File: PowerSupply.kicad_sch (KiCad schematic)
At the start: 9 parts, among them Q1 DMP2160UW-7, U1 MIC2288YD5-TR

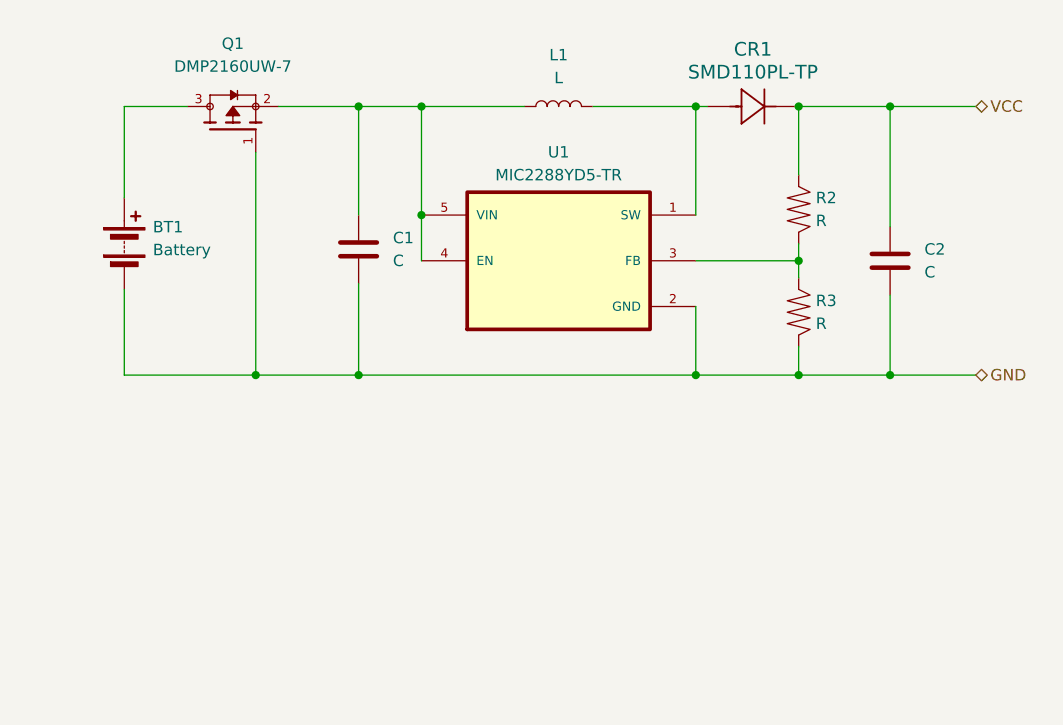
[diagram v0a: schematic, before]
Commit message: 2 voltage regulators + new diodes
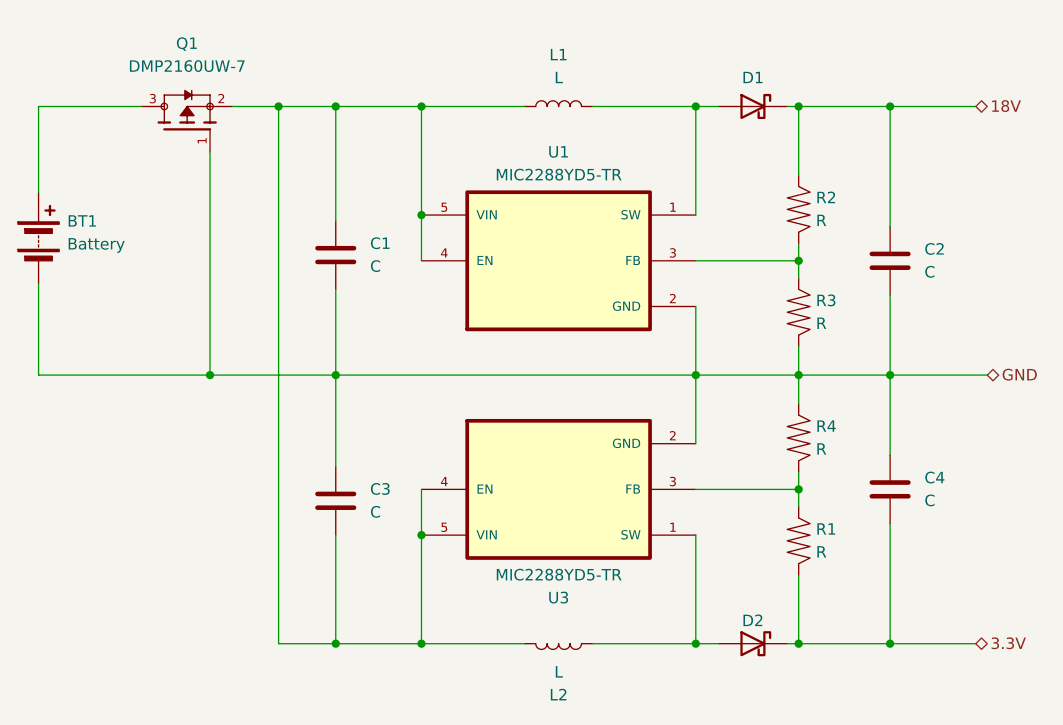
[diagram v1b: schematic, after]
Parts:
- removed CR1: SMD110PL-TP, SOD-123FL_MCC, symbol ProjDiode:SMD110PL-TP
- added C3, C4: C, symbol Hestres_Standard_Lib:C
- added D1, D2: D_Schottky, symbol Hestres_Standard_Lib:D_Schottky
- added L2: L, symbol Hestres_Standard_Lib:L
- added R1, R4: R, symbol Hestres_Standard_Lib:R
- added U3: MIC2288YD5-TR, MIC2288YD5-TR:SOT95P280X100-5N, symbol MIC2288YD5-TR:MIC2288YD5-TR
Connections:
- net GND: now also C3.1, C4.1, R4.1, U3.2 (GND)
- net at C1.1, L1.1, Q1.2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: now also C3.2, L2.1, U3.4 (EN), U3.5 (VIN)
- net at L1.2, U1.1 (SW): now also D1.2 (A)
- net VCC renamed 18V
- net 18V: now also D1.1 (K)
- new net: D2.2 (A), L2.2, U3.1 (SW)
- new net: R1.1, R4.2, U3.3 (FB)
- new net 3.3V: C4.2, D2.1 (K), R1.2
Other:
- moved on the sheet: BT1, C1, Q1

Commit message: Capacitors chosen and footprints assigned
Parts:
- C1, C3: value C -> 1uF; footprint (none) -> Capacitor_SMD:C_0805_2012Metric
- C2, C4: value C -> 4.7 uF; footprint (none) -> Capacitor_SMD:C_0805_2012Metric
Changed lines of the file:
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@@
   (symbol (lib_id "Hestres_Standard_Lib:C") (at 109.855 73.025 0) (unit 1)
     (in_bom yes) (on_board yes) (dnp no) (fields_autoplaced)
-    (property "Reference" "C1" (at 113.665 71.755 0)
+    (property "Reference" "C1" (at 113.03 71.755 0)
       (effects (font (size 1.27 1.27)) (justify left))
     )
-    (property "Value" "C" (at 113.665 74.295 0)
+    (property "Value" "1uF" (at 113.03 74.295 0)
       (effects (font (size 1.27 1.27)) (justify left))
     )
-    (property "Footprint" "" (at 110.8202 76.835 0)
+    (property "Footprint" "Capacitor_SMD:C_0805_2012Metric" (at 110.8202 76.835 0)
       (effects (font (size 1.27 1.27)) hide)
     )
@@
       (effects (font (size 1.27 1.27)) (justify left))
     )
-    (property "Value" "C" (at 175.26 100.33 0)
+    (property "Value" "4.7 uF" (at 175.26 100.33 0)
       (effects (font (size 1.27 1.27)) (justify left))
     )
-    (property "Footprint" "" (at 172.4152 102.87 0)
+    (property "Footprint" "Capacitor_SMD:C_0805_2012Metric" (at 172.4152 102.87 0)
       (effects (font (size 1.27 1.27)) hide)
     )
@@
       (effects (font (size 1.27 1.27)) (justify left))
     )
-    (property "Value" "C" (at 175.26 74.93 0)
+    (property "Value" "4.7 uF" (at 175.26 74.93 0)
       (effects (font (size 1.27 1.27)) (justify left))
     )
-    (property "Footprint" "" (at 172.4152 77.47 0)
+    (property "Footprint" "Capacitor_SMD:C_0805_2012Metric" (at 172.4152 77.47 0)
       (effects (font (size 1.27 1.27)) hide)
     )
@@
       (effects (font (size 1.27 1.27)) (justify left))
     )
-    (property "Value" "C" (at 113.665 101.6 0)
+    (property "Value" "1uF" (at 113.665 101.6 0)
       (effects (font (size 1.27 1.27)) (justify left))
     )
-    (property "Footprint" "" (at 110.8202 104.14 0)
+    (property "Footprint" "Capacitor_SMD:C_0805_2012Metric" (at 110.8202 104.14 0)
       (effects (font (size 1.27 1.27)) hide)
     )

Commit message: Resistors named, footprints assigned
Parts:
- R1: value R -> 3.3HI; footprint (none) -> Resistor_SMD:R_0805_2012Metric
- R2: value R -> 18HI; footprint (none) -> Resistor_SMD:R_0805_2012Metric
- R3: value R -> 18LO; footprint (none) -> Resistor_SMD:R_0805_2012Metric
- R4: value R -> 3.3LO; footprint (none) -> Resistor_SMD:R_0805_2012Metric
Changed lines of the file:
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@@
       (effects (font (size 1.27 1.27)) (justify left))
     )
-    (property "Value" "R" (at 163.195 106.045 0)
+    (property "Value" "3.3HI" (at 163.195 106.045 0)
       (effects (font (size 1.27 1.27)) (justify left))
     )
-    (property "Footprint" "" (at 159.512 104.775 90)
+    (property "Footprint" "Resistor_SMD:R_0805_2012Metric" (at 159.512 104.775 90)
       (effects (font (size 1.27 1.27)) hide)
     )
@@
   (symbol (lib_id "Hestres_Standard_Lib:R") (at 161.29 67.945 0) (unit 1)
     (in_bom yes) (on_board yes) (dnp no) (fields_autoplaced)
-    (property "Reference" "R2" (at 163.195 66.675 0)
+    (property "Reference" "R2" (at 163.83 66.675 0)
       (effects (font (size 1.27 1.27)) (justify left))
     )
-    (property "Value" "R" (at 163.195 69.215 0)
+    (property "Value" "18HI" (at 163.83 69.215 0)
       (effects (font (size 1.27 1.27)) (justify left))
     )
-    (property "Footprint" "" (at 159.512 67.945 90)
+    (property "Footprint" "Resistor_SMD:R_0805_2012Metric" (at 159.512 67.945 90)
       (effects (font (size 1.27 1.27)) hide)
     )
@@
       (effects (font (size 1.27 1.27)) (justify left))
     )
-    (property "Value" "R" (at 163.195 94.615 0)
+    (property "Value" "3.3LO" (at 163.195 94.615 0)
       (effects (font (size 1.27 1.27)) (justify left))
     )
-    (property "Footprint" "" (at 159.512 93.345 90)
+    (property "Footprint" "Resistor_SMD:R_0805_2012Metric" (at 159.512 93.345 90)
       (effects (font (size 1.27 1.27)) hide)
     )
@@
   (symbol (lib_id "Hestres_Standard_Lib:R") (at 161.29 79.375 0) (unit 1)
     (in_bom yes) (on_board yes) (dnp no) (fields_autoplaced)
-    (property "Reference" "R3" (at 163.195 78.105 0)
+    (property "Reference" "R3" (at 163.83 78.105 0)
       (effects (font (size 1.27 1.27)) (justify left))
     )
-    (property "Value" "R" (at 163.195 80.645 0)
+    (property "Value" "18LO" (at 163.83 80.645 0)
       (effects (font (size 1.27 1.27)) (justify left))
     )
-    (property "Footprint" "" (at 159.512 79.375 90)
+    (property "Footprint" "Resistor_SMD:R_0805_2012Metric" (at 159.512 79.375 90)
       (effects (font (size 1.27 1.27)) hide)
     )

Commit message: Inductor chosen and footprint assigned
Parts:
- L1, L2: value L -> 10uH; footprint (none) -> Proj:IND_TAIYO_NR6028_TAY
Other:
- moved on the sheet: L2
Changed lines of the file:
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@@
   (junction (at 109.855 116.205) (diameter 0) (color 0 0 0 0)
   )
-  (junction (at 103.505 56.515) (diameter 0) (color 0 0 0 0)
-  )
   (junction (at 161.29 86.36) (diameter 0) (color 0 0 0 0)
   )
@@
   (junction (at 171.45 116.205) (diameter 0) (color 0 0 0 0)
   )
+  (junction (at 102.87 56.515) (diameter 0) (color 0 0 0 0)
+  )
   (junction (at 171.45 86.36) (diameter 0) (color 0 0 0 0)
   )
@@
     (stroke (width 0) (type default))
   )
-  (wire (pts (xy 103.505 56.515) (xy 109.855 56.515))
+  (wire (pts (xy 102.87 56.515) (xy 109.855 56.515))
     (stroke (width 0) (type default))
   )
@@
     (stroke (width 0) (type default))
   )
-  (wire (pts (xy 103.505 116.205) (xy 109.855 116.205))
+  (wire (pts (xy 102.87 116.205) (xy 109.855 116.205))
     (stroke (width 0) (type default))
   )
@@
     (stroke (width 0) (type default))
   )
-  (wire (pts (xy 98.425 56.515) (xy 103.505 56.515))
+  (wire (pts (xy 98.425 56.515) (xy 102.87 56.515))
+    (stroke (width 0) (type default))
+  )
+  (wire (pts (xy 102.87 56.515) (xy 102.87 116.205))
     (stroke (width 0) (type default))
   )
   (wire (pts (xy 171.45 116.205) (xy 180.975 116.205))
-    (stroke (width 0) (type default))
-  )
-  (wire (pts (xy 103.505 56.515) (xy 103.505 116.205))
     (stroke (width 0) (type default))
   )
@@
   )
   (symbol (lib_id "MIC2288YD5-TR:MIC2288YD5-TR") (at 134.62 99.06 0) (mirror x) (unit 1)
-    (in_bom yes) (on_board yes) (dnp no) (fields_autoplaced)
-    (property "Reference" "U3" (at 134.62 111.125 0)
-      (effects (font (size 1.27 1.27)))
-    )
-    (property "Value" "MIC2288YD5-TR" (at 134.62 108.585 0)
+    (in_bom yes) (on_board yes) (dnp no)
+    (property "Reference" "U3" (at 134.62 88.265 0)
+      (effects (font (size 1.27 1.27)))
+    )
+    (property "Value" "MIC2288YD5-TR" (at 134.62 90.17 0)
       (effects (font (size 1.27 1.27)))
     )
@@
     )
   )
-  (symbol (lib_id "Hestres_Standard_Lib:L") (at 134.62 116.205 90) (mirror x) (unit 1)
-    (in_bom yes) (on_board yes) (dnp no) (fields_autoplaced)
-    (property "Reference" "L2" (at 134.62 121.92 90)
-      (effects (font (size 1.27 1.27)))
-    )
-    (property "Value" "L" (at 134.62 119.38 90)
-      (effects (font (size 1.27 1.27)))
-    )
-    (property "Footprint" "" (at 134.62 116.205 0)
+  (symbol (lib_id "Hestres_Standard_Lib:L") (at 134.62 116.205 90) (unit 1)
+    (in_bom yes) (on_board yes) (dnp no)
+    (property "Reference" "L2" (at 134.62 110.49 90)
+      (effects (font (size 1.27 1.27)))
+    )
+    (property "Value" "10uH" (at 134.62 113.03 90)
+      (effects (font (size 1.27 1.27)))
+    )
+    (property "Footprint" "Proj:IND_TAIYO_NR6028_TAY" (at 134.62 116.205 0)
       (effects (font (size 1.27 1.27)) hide)
     )
@@
       (effects (font (size 1.27 1.27)))
     )
-    (property "Value" "L" (at 134.62 53.34 90)
-      (effects (font (size 1.27 1.27)))
-    )
-    (property "Footprint" "" (at 134.62 56.515 0)
-      (effects (font (size 1.27 1.27)) hide)
-    )
+    (property "Value" "10uH" (at 134.62 53.34 90)
+      (effects (font (size 1.27 1.27)))
+    )
+    (property "Footprint" "Proj:IND_TAIYO_NR6028_TAY" (at 134.62 56.515 0)
+      (effects (font (size 1.27 1.27)) hide)
+    )
